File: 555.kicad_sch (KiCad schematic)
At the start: 2 parts, among them U1 NE555P

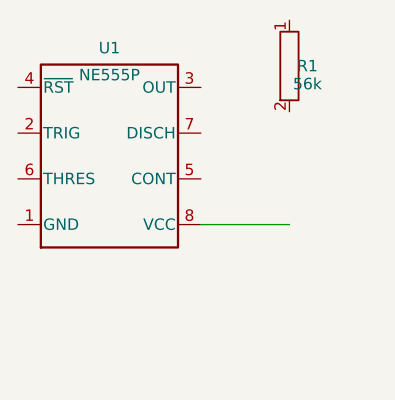
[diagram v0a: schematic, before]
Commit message: Implement 555 timer project from GEMINI.md
This commit completes the implementation of a 555 timer blinking LED board.
Target frequency: 1Hz, Duty cycle: 30% active (using active-low LED).

Includes:
- /specifications: NE555, LED, and KiCAD IPC API docs.
- /docs: IPC development transcript.
- generate_schematic.py: SKiDL script for netlist generation.
- generate_pcb.py: Python script for component placement and routing (0 unconnected pads).
- KiCad project files: 555.kicad_sch, 555.kicad_pcb, 555.kicad_pro, 555.kicad_prl.
- Documentation: DECICISON_LOG.md, FAILD_ATTEMPTS.md, KICAD_IPC_CALLS.md.
- CI/CD: .github/workflows/check.yml for automated hardware verification.
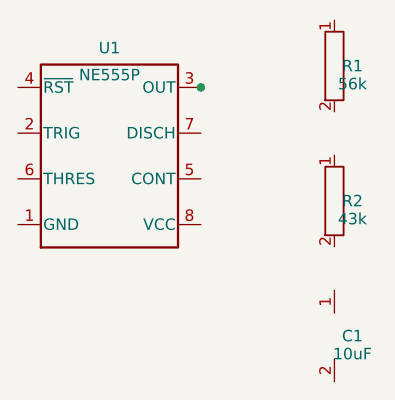
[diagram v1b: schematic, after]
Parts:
- added C1: 10uF, Capacitor_SMD:CP_Elec_4x5.4, symbol Device:C_Polarized
- added R2: 43k, Resistor_SMD:R_0805_2012Metric, symbol Device:R
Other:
- moved on the sheet: R1
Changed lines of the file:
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@@
 		(property "Footprint" "Package_DIP:DIP-8_W7.62mm" (at 100 112 0) (effects (font (size 1.27 1.27)) hide))
 	)
-	(symbol (lib_id "Device:R") (at 120 90 0) (unit 1)
+	(symbol (lib_id "Device:R") (at 125 90 0) (unit 1)
 		(in_bom yes) (on_board yes) (dnp no) (uuid "r1-0000-0000-0000-000000000001")
-		(property "Reference" "R1" (at 122 90 0) (effects (font (size 1.27 1.27))))
-		(property "Value" "56k" (at 122 92 0) (effects (font (size 1.27 1.27))))
-		(property "Footprint" "Resistor_SMD:R_0805_2012Metric" (at 120 90 0) (effects (font (size 1.27 1.27)) hide))
+		(property "Reference" "R1" (at 127 90 0) (effects (font (size 1.27 1.27))))
+		(property "Value" "56k" (at 127 92 0) (effects (font (size 1.27 1.27))))
+		(property "Footprint" "Resistor_SMD:R_0805_2012Metric" (at 125 90 0) (effects (font (size 1.27 1.27)) hide))
 	)
-	(wire (pts (xy 110.16 107.62) (xy 120 107.62)) (stroke (width 0) (type default)) (uuid "w1-0000-0000-0000-000000000001"))
+	(symbol (lib_id "Device:R") (at 125 105 0) (unit 1)
+		(in_bom yes) (on_board yes) (dnp no) (uuid "r2-0000-0000-0000-000000000001")
+		(property "Reference" "R2" (at 127 105 0) (effects (font (size 1.27 1.27))))
+		(property "Value" "43k" (at 127 107 0) (effects (font (size 1.27 1.27))))
+		(property "Footprint" "Resistor_SMD:R_0805_2012Metric" (at 125 105 0) (effects (font (size 1.27 1.27)) hide))
+	)
+	(symbol (lib_id "Device:C_Polarized") (at 125 120 0) (unit 1)
+		(in_bom yes) (on_board yes) (dnp no)
+		(property "Reference" "C1" (at 127 120 0) (effects (font (size 1.27 1.27))))
+		(property "Value" "10uF" (at 127 122 0) (effects (font (size 1.27 1.27))))
+		(property "Footprint" "Capacitor_SMD:CP_Elec_4x5.4" (at 125 120 0) (effects (font (size 1.27 1.27)) hide))
+	)
+	(junction (at 110.16 92.38) (diameter 0) (color 0 0 0 0) (uuid "j1-0000-0000-0000-000000000001"))
 )
